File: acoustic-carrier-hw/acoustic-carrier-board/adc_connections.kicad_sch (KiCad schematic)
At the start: 28 parts, among them IC1 ECP5-BGA256, J2 Conn_02x08_Odd_Even, U7 MS9280

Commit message: [carrier] Reorganized schematic, moPut adc signals in bus, fixed DRC errors (next) recheck ethernet, check usb, add power switch
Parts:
- added C108: 10uF, Capacitor_SMD:C_0603_1608Metric, symbol Device:C_Small
- added C109, C136: 0.1uF, Capacitor_SMD:C_0402_1005Metric, symbol Device:C_Small
- added C110: 10nF, Capacitor_SMD:C_0402_1005Metric, symbol Device:C_Small
- added C111, C115, C133: 10pF, Capacitor_SMD:C_0603_1608Metric, symbol Device:C_Small
- added C134, C135: 100 nF +-5%, Capacitor_SMD:C_0603_1608Metric_Pad1.08x0.95mm_HandSolder, symbol Device:C_Small
- added C142: 220nF, Capacitor_SMD:C_0402_1005Metric, symbol Device:C_Small
- added J15, J17, J18, J19, J20, J21, J4: BWU.FL-IPEX1, fpga:BWU.FL-IPEX1, symbol Connector:Conn_Coaxial_Small
- added J22: 8P8C_Shielded, Connector_RJ:RJ45_RCH_RC01937, symbol Connector:8P8C_Shielded
- added R125: 0, Resistor_SMD:R_0603_1608Metric_Pad0.98x0.95mm_HandSolder, symbol Device:R_Small
- added R126, R127, R128, R129: 470, Resistor_SMD:R_0603_1608Metric, symbol Device:R_Small
- added R130, R134, R135, R136, R138, R140, R141, R143, R145, R146: 0, Resistor_SMD:R_0603_1608Metric, symbol Device:R_Small
- added R131, R133, R147, R148, R150, R151: 10k, Resistor_SMD:R_0603_1608Metric, symbol Device:R_Small
- added R132, R137, R144, R149, R152, R154, R156, R157: 1k, Resistor_SMD:R_0603_1608Metric, symbol Device:R_Small
- added R139, R142: 47, Resistor_SMD:R_0603_1608Metric, symbol Device:R_Small
- added R153: 75, Resistor_SMD:R_0603_1608Metric, symbol Device:R_Small
- added R155: 1.5k, Resistor_SMD:R_0603_1608Metric, symbol Device:R_Small
- added R158: 4.7k, Resistor_SMD:R_0603_1608Metric, symbol Device:R_Small
- added RJ2: HR913550A, rj45:RJ45-TH_HR913550A, symbol RJ45_HR913550A:HR913550A
- added TP13, TP14, TP15, TP16, TP17: TestPoint_Small, TestPoint:TestPoint_Pad_D1.5mm, symbol Connector:TestPoint_Small
- added U20: THS4521IDGK, Package_SO:VSSOP-8_3x3mm_P0.65mm, symbol Amplifier_Difference:THS4521IDGK
- added U21: DGQ2788AEN-T1-GE4, fpga:QFN40P260X180X60-16N_Fv1.2, symbol DGQ2788AEN:DGQ2788AEN-T1-GE4
- added U22: LMV321, Package_TO_SOT_SMD:SOT-23-5, symbol Amplifier_Operational:LMV321
- added U23: TL432DBZ, Package_TO_SOT_SMD:SOT-23, symbol Reference_Voltage:TL432DBZ
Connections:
- net ADC_AIN+: now also C115.2, R135.1, R140.1
- net ADC_AIN-: now also C115.1, R143.1, R145.1
- net ADC_IN12_SW: now also IC1.E6 (PT20A), U21.14 (IN1-2); no longer IC1.A7 (PT29A/PCLKT0_0)
- net FPGA_LED0: now also R128.2, R129.2
- net FPGA_LED1: now also R126.2, R127.1
- net GND: now also C108.2, C109.2, C110.2, C136.2, C142.1, J15.2 (Ext), J17.2 (Ext), J18.2 (Ext), J19.2 (Ext), J20.2 (Ext), J21.2 (Ext), J22.SH, J4.2 (Ext), R125.1, R127.2, R129.1, R156.1, R157.2, R158.2, RJ2.5, RJ2.8 (GND), U20.6 (V_{S-}), U21.2 (GND), U22.2 (V-), U23.3 (A)
- net VCORE_3V3: now also C108.1, C109.1, C110.1, C136.1, R138.2, RJ2.12, RJ2.9, U20.3 (V_{S+}), U22.5 (V+)
- net VDDA: now also R152.1, R154.1, U21.10 (V+)
- net SIG.T_SDA: now reaches IC1.A8 (PT29B/PCLKC0_0)
- net SIG.T_SDA: now also J2.15 (Pin_15)
- net FPGA_ADC_CLK renamed FPGA_ADC.CLK
- net FPGA_ADC_D0 renamed FPGA_ADC.D0
- net FPGA_ADC_D1 renamed FPGA_ADC.D1
- net FPGA_ADC_D2 renamed FPGA_ADC.D2
- net FPGA_ADC_D3 renamed FPGA_ADC.D3
- net FPGA_ADC_D4 renamed FPGA_ADC.D4
- net FPGA_ADC_D5 renamed FPGA_ADC.D5
- net FPGA_ADC_D6 renamed FPGA_ADC.D6
- net FPGA_ADC_D7 renamed FPGA_ADC.D7
- net FPGA_ADC_D8 renamed FPGA_ADC.D8
- net FPGA_ADC_D9 renamed FPGA_ADC.D9
- net FPGA_ADC_OTR renamed FPGA_ADC.OTR
- net SIG_B40V_EN: no longer names the net of IC1.D6 (PT20B)
- net SIG_B40V_EN: no longer J2.11 (Pin_11)
- net SIG_PWM0 renamed SIG.PWM0
- net SIG_PWM1 renamed SIG.PWM1
- net SIG_PWM2 renamed SIG.PWM2
- net SIG_PWM3 renamed SIG.PWM3
- net SIG_S10V_EN renamed SIG.S10V_EN
- net SIG.S10V_EN: now also IC1.C7 (PT27A/PCLKT0_1); no longer IC1.E6 (PT20A)
- net SIG_T_SCL renamed SIG.T_SCL
- net SIG.T_SCL: now also IC1.A7 (PT29A/PCLKT0_0); no longer IC1.C7 (PT27A/PCLKT0_1)
- net SIG_T_SDA renamed SIG.B40_EN
- net SIG.B40_EN: now also J2.11 (Pin_11); no longer J2.15 (Pin_15)
- new net: R155.2, R158.1, U23.1 (REF)
- new net: J19.1 (In), U21.4 (COM3)
- new net: J15.1 (In), R133.2, R135.2
- new net: R134.2, R136.1, R137.2
- new net: R136.2, U21.12 (COM1)
- new net: RJ2.3, TP13.1
- new net: C133.1, R144.1, R149.1, U20.1 (-)
- new net: C133.2, R142.2, U20.4
- new net: C111.1, R139.2, U20.5
- new net: R138.1, U20.7 (~{PD})
- new net: C111.2, R132.2, R137.1, U20.8 (+)
- new net: C134.2, R150.2, U21.11 (NO1)
- new net: R141.1, R144.2, R146.1
- new net: R141.2, U21.16 (COM2)
- new net: J4.1 (In), R131.2, R134.1
- new net: R132.1, R139.1, R140.2
- new net: C134.1, J22.5
- new net: RJ2.2, U21.1 (NC2)
- new net: RJ2.1, U21.13 (NC1)
- new net: C135.2, R151.1, U21.15 (NO2)
- new net: J18.1 (In), U21.3 (NO3)
- new net: J17.1 (In), U21.5 (NC3)
- new net: TP15.1, U21.6 (IN3-4)
- new net: RJ2.6, TP14.1
- new net: J20.1 (In), R145.2, R147.2
- new net: R125.2, RJ2.13, RJ2.14
- new net: R142.1, R143.2, R149.2
- new net: J21.1 (In), R146.2, R148.2
- new net: R130.2, RJ2.4
- new net: J22.2, TP16.1
- new net: R128.1, RJ2.10
- new net: R126.1, RJ2.11
- new net: R153.2, R156.2, U22.3 (-), U22.4
- new net: J22.1, TP17.1
- new net: C135.1, J22.4
- new net ADC_VOCM_BUFF: C142.2, R130.1, R131.1, R133.1, R147.1, R148.1, R150.1, R151.2, R153.1, U20.2 (V_{OCM})
- new net ADC_VOCM_REF: R152.2, R154.2, R155.1, R157.1, U22.1 (+), U23.2 (K)
- no-connect marks 1 -> 9
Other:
- note added: "- Ethernet magnetics by default for decoupling Layout of transition between 2 ADC-inputs: - Use 0-ohm resistor to cross lower trace (instead of jumpers for signal integrity) LEDS: - Current through leds (3.3 - 2.2) / 2e3 = 0.55 mA (voltage drop 1.8-2.8 V) - Differential impedance: 100 ohms - Input capacitance: 100 nF, f_plateau = 1/[2*pi*C*(R_diff/2)] = 30 kHz Pin 13, 14: shield / frame connection"
- note added: "ADC CONNECTORS"
- note added: "ADC Filter - Optimize later with signal generator + measurements - Input impedance (max 100 kOhm) >>> then source (100 ohm)"
- note added: "ADC INPUT BUFFER"
- note added: "ADC LOW PASS FILTER"
- note added: "ADC SWITCH"
- note added: "Current requirement in nA - Current limiting resistor -> smaller = less noise -> larger = less energy wasting - Reference input current: 0.6 uA - 3.3e-3 / (1+1.5+4.7) = 532 uA through biasing resistors - (3.3-1.65) / 1k = 1.65 mA flowing through the Cathode"
- note added: "Secondary voltage divider reference (just in case the reference doesn't work)"
- note added: "Test connector Make stub as short as possible"
- note added: "VOCM REFERENCE BUFFERING"
- note added: "VOCM REFERENCE GENERATION"
- note added: "VOCM buffering - Reducing source impedance of resistive divider - buffer configuration for OPAMP to drive COMP pin - Damping resistor added at output due to big capacitive load - Maximum output current: 5-40 mA - Maximum current: 1.6 V / 75 ohms = 21.33 mA Differential mode biasing - 10 kOhm, 0.80 uA input bias for ths4521 -> 10e3 * 0.80e-6 = 8 mV offset at worst Use LMV321 - Higher current than 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"
- note added: "Voltage reference: 1.25 Target voltage: 1.65 So Vtarget * [R1/(R1+R2)]= Vref - R1: 1.5k, R2: 4.6k - Vref * R1/(R1+R2) = Vtarget * [4.6/(1.5+4.6)] = Vref - Deviation from 1.25: (1.25-1.244/1.25) = 0.48%"
- moved on the sheet: C86, C87, C88, C89, C90, C91, C92, C93, C94, C95, IC1B, J2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

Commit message: [carrier] Fixed error in ethernet power supply, separated footprints + symbols into library (next) check whether supply should be DVDDH
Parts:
- removed IC1: ECP5-BGA256, fpga:BGA256C80P16X16_1400X1400X170, symbol ecp5bga256:ECP5-BGA256
- removed J15, J18, J19, J20, J21: BWU.FL-IPEX1, fpga:BWU.FL-IPEX1, symbol Connector:Conn_Coaxial_Small
- removed RJ2: HR913550A, rj45:RJ45-TH_HR913550A, symbol RJ45_HR913550A:HR913550A
- removed U21: DGQ2788AEN-T1-GE4, fpga:QFN40P260X180X60-16N_Fv1.2, symbol DGQ2788AEN:DGQ2788AEN-T1-GE4
- removed U7: MS9280, Package_SO:SSOP-28_5.3x10.2mm_P0.65mm, symbol ms9280:MS9280
- added IC1: ECP5-BGA256, iw-fpga_mcu:BGA256C80P16X16_1400X1400X170, symbol iw-fpga_mcu:ECP5-BGA256
- added J1, J10, J11, J5, J7: BWU.FL-IPEX1, iw-connector:BWU.FL-IPEX1, symbol Connector:Conn_Coaxial_Small
- added RJ1: HR913550A, iw-connector:RJ45-TH_HR913550A, symbol iw-connector:HR913550A
- added U2: DGQ2788AEN-T1-GE4, iw-analog:QFN40P260X180X60-16N_Fv1.2, symbol iw-analog:DGQ2788AEN-T1-GE4
- added U3: MS9280, Package_SO:SSOP-28_5.3x10.2mm_P0.65mm, symbol iw-analog:MS9280
- J17, J4: footprint fpga:BWU.FL-IPEX1 -> iw-connector:BWU.FL-IPEX1
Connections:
- net ADC_AIN+: now also U3.27 (AIN)
- net ADC_IN12_SW: now also IC1.E6 (PT20A), U2.14 (IN1-2)
- net ADC_MODE: now also U3.23 (MODE)
- net ADC_REFBF: now also U3.24 (REFBF)
- net ADC_REFBS: now also U3.25 (REFBS)
- net ADC_REFSENSE: now also U3.18 (REFSENSE)
- net ADC_REFTF: now also U3.22 (REFTF)
- net ADC_REFTS: now also U3.21 (REFTS)
- net ADC_VREF: now also U3.26 (VREF)
- net FPGA_ADC.CLK: now also IC1.A2 (PT4A), U3.15 (CLK)
- net FPGA_ADC.D0: now also IC1.B3 (PT4B), U3.3 (D0)
- net FPGA_ADC.D1: now also IC1.A3 (PT6A), U3.4 (D1)
- net FPGA_ADC.D2: now also IC1.A4 (PT6B), U3.5 (D2)
- net FPGA_ADC.D3: now also IC1.E4 (PT9A), U3.6 (D3)
- net FPGA_ADC.D4: now also IC1.D4 (PT9B), U3.7 (D4)
- net FPGA_ADC.D5: now also IC1.C4 (PT11A), U3.8 (D5)
- net FPGA_ADC.D6: now also IC1.B4 (PT11B), U3.9 (D6)
- net FPGA_ADC.D7: now also IC1.E5 (PT13A), U3.10 (D7)
- net FPGA_ADC.D8: now also IC1.D5 (PT13B), U3.11 (D8)
- net FPGA_ADC.D9: now also IC1.C5 (PT15A), U3.12 (D9)
- net FPGA_ADC.OTR: now also IC1.B5 (PT15B), U3.13 (OTR)
- net FPGA_LED0: now also IC1.A6 (PT18B)
- net FPGA_LED1: now also IC1.A5 (PT18A)
- net GND: now also J1.2 (Ext), J10.2 (Ext), J11.2 (Ext), J5.2 (Ext), J7.2 (Ext), RJ1.5, RJ1.8 (GND), U2.2 (GND), U3.1 (AVSS), U3.14 (DRVSS), U3.19 (CLAMP)
- net SIG.B40_EN: now also IC1.B7 (PT27B/PCLKC0_1)
- net SIG.PWM0: now also IC1.C6 (PT22A)
- net SIG.PWM1: now also IC1.B6 (PT22B)
- net SIG.PWM2: now also IC1.E7 (PT24A/GR_PCLK0_1)
- net SIG.PWM3: now also IC1.D7 (PT24B/GR_PCLK0_0)
- net SIG.S10V_EN: now also IC1.C7 (PT27A/PCLKT0_1)
- net SIG.T_SCL: now also IC1.A7 (PT29A/PCLKT0_0)
- net SIG.T_SDA: now also IC1.A8 (PT29B/PCLKC0_0)
- net VCORE_3V3: now also IC1.F6 (VCCIO0_1), IC1.F7 (VCCIO0_2), RJ1.12, RJ1.9, U3.2 (DRVDD)
- net VDDA: now also U2.10 (V+), U3.28 (AVDD)
- net at R133.2, R135.2: now also J10.1 (In)
- net at R136.2: now also U2.12 (COM1)
- net at TP13.1: now also RJ1.3
- net at C134.2, R150.2: now also U2.11 (NO1)
- net at R141.2: now also U2.16 (COM2)
- net at R79.2: now also U3.20 (CLAMPIN)
- net at JP6.2 (B): now also U3.16 (TRISTATE), U3.17 (STBY)
- net at C135.2, R151.1: now also U2.15 (NO2)
- net at J17.1 (In): now also U2.5 (NC3)
- net at TP15.1: now also U2.6 (IN3-4)
- net at TP14.1: now also RJ1.6
- net at R145.2, R147.2: now also J11.1 (In)
- net at R125.2: now also RJ1.13, RJ1.14
- net at R146.2, R148.2: now also J7.1 (In)
- net at R130.2: now also RJ1.4
- net at R128.1: now also RJ1.10
- net at R126.1: now also RJ1.11
- new net: RJ1.1, U2.13 (NC1)
- new net: RJ1.2, U2.1 (NC2)
- new net: J5.1 (In), U2.4 (COM3)
- new net: J1.1 (In), U2.3 (NO3)
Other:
- moved on the sheet: C134, C135, J22, R150, R151, TP16, TP17

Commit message: [carrier] Signal switch-around in ddr3
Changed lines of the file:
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@@
 	(wire
 		(pts
-			(xy 142.24 212.09) (xy 142.24 210.82)
+			(xy 142.24 212.09) (xy 142.24 215.9)
 		)
 		(stroke
@@
 		)
 		(property "Value" "100 nF +-5%"
-			(at 54.102 109.22 90)
+			(at 49.022 122.174 0)
 			(effects
 				(font
@@
 		(dnp no)
 		(property "Reference" "C135"
-			(at 45.466 122.428 0)
+			(at 47.498 126.492 0)
 			(effects
 				(font
@@
 		)
 		(property "Value" "100 nF +-5%"
-			(at 54.102 116.84 90)
+			(at 41.402 132.588 0)
 			(effects
 				(font
@@
 	(symbol
 		(lib_id "power:GND")
-		(at 142.24 210.82 180)
+		(at 142.24 215.9 0)
 		(unit 1)
 		(exclude_from_sim no)
@@
 		(dnp no)
 		(property "Reference" "#PWR030"
-			(at 142.24 204.47 0)
+			(at 142.24 222.25 0)
 			(effects
 				(font
@@
 		)
 		(property "Value" "GND"
-			(at 146.05 209.804 0)
+			(at 138.43 216.916 0)
 			(effects
 				(font
@@
 		)
 		(property "Footprint" ""
-			(at 142.24 210.82 0)
+			(at 142.24 215.9 0)
 			(effects
 				(font
@@
 		)
 		(property "Datasheet" ""
-			(at 142.24 210.82 0)
+			(at 142.24 215.9 0)
 			(effects
 				(font
@@
 		)
 		(property "Description" "Power symbol creates a global label with name \"GND\" , ground"
-			(at 142.24 210.82 0)
+			(at 142.24 215.9 0)
 			(effects
 				(font

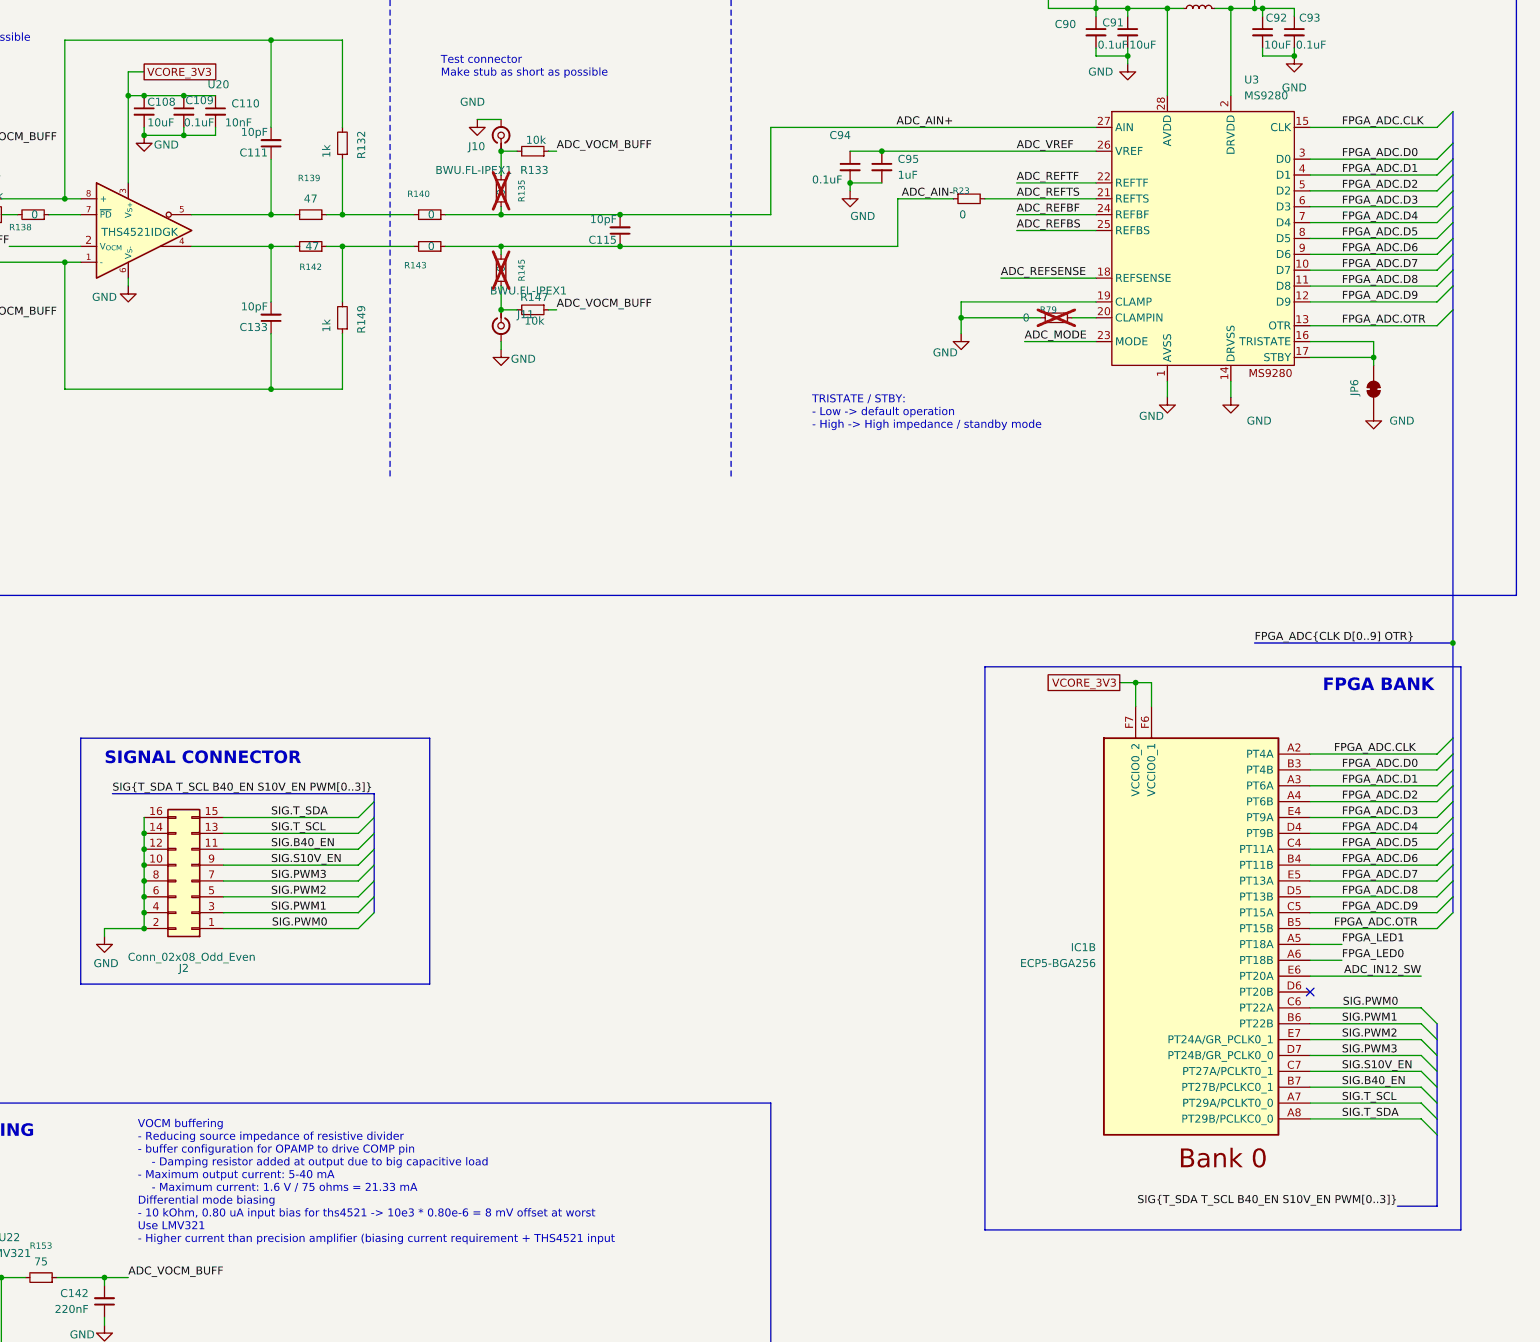
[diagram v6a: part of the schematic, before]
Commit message: [¢arrier] Fixed busses, added resistive arrays instead of 4x4k7 or 4x10k
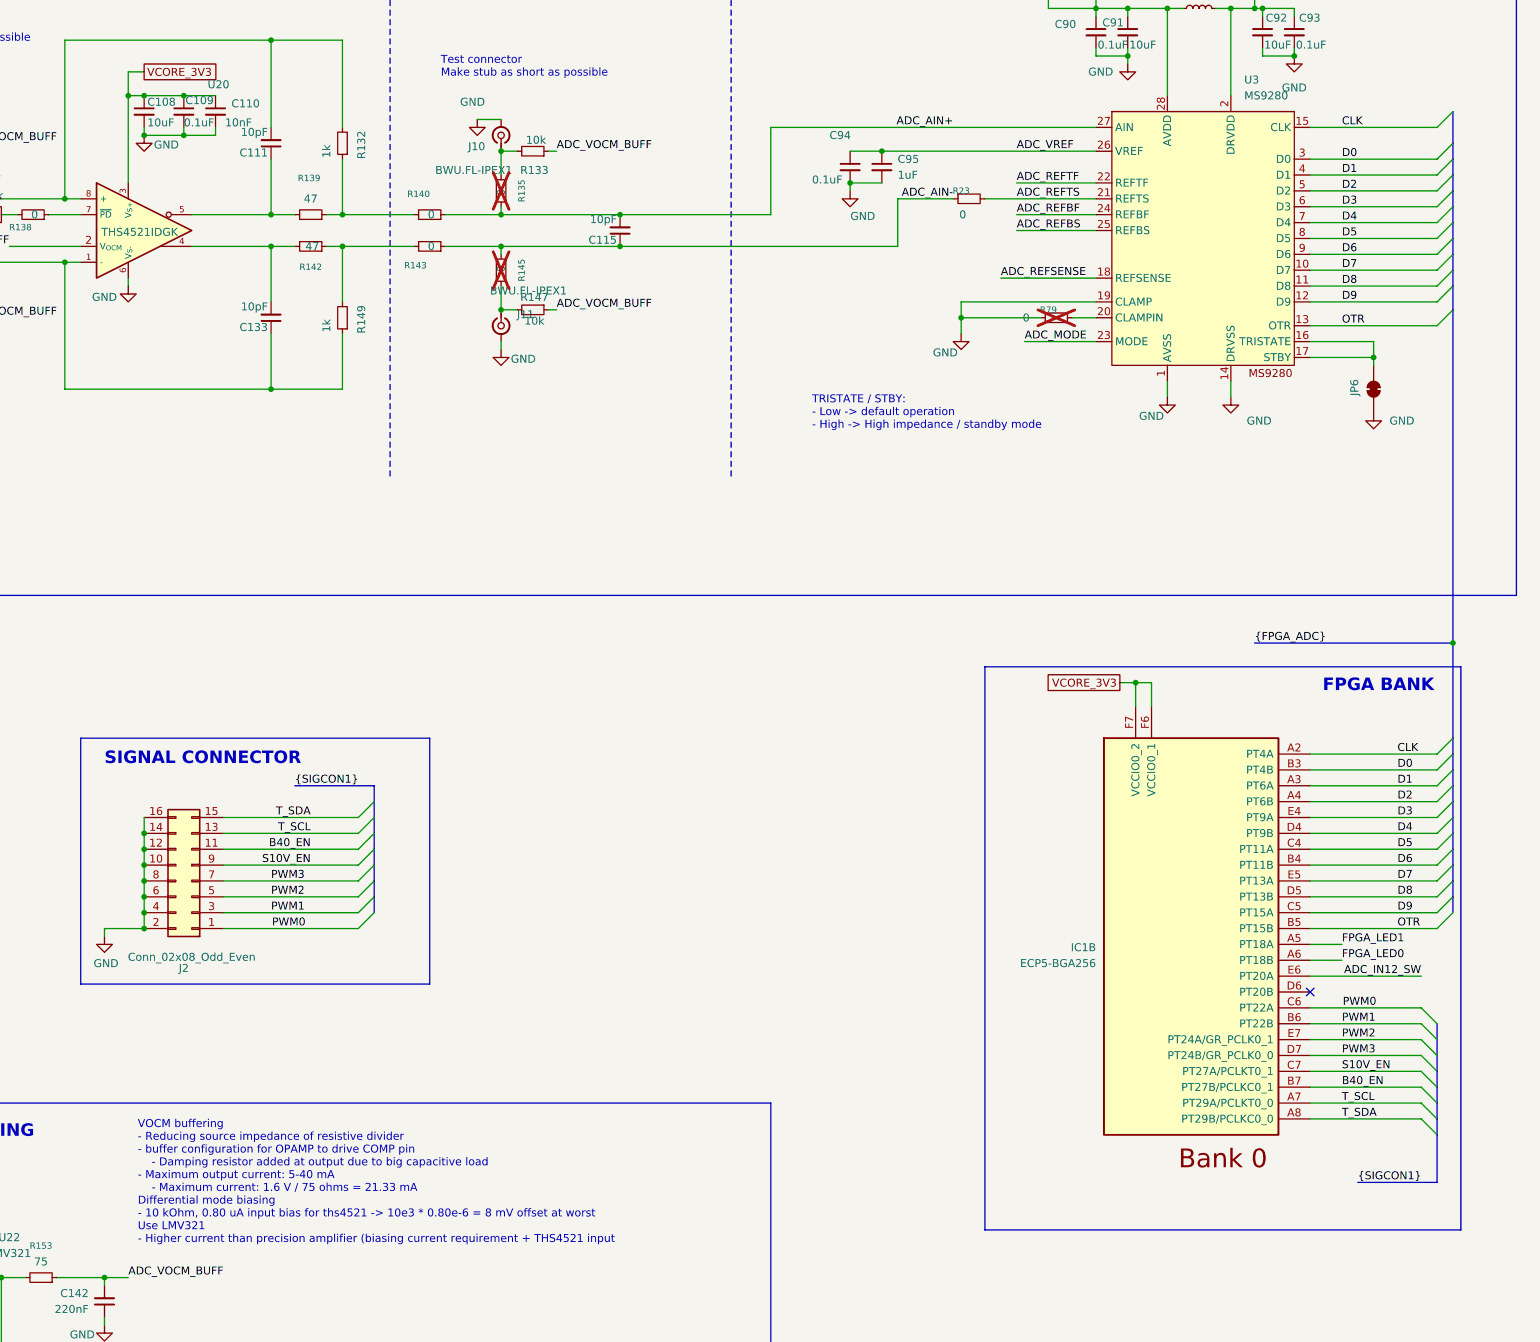
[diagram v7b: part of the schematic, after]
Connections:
- net FPGA_ADC.CLK renamed CLK
- net FPGA_ADC.D0 renamed D0
- net FPGA_ADC.D1 renamed D1
- net FPGA_ADC.D2 renamed D2
- net FPGA_ADC.D3 renamed D3
- net FPGA_ADC.D4 renamed D4
- net FPGA_ADC.D5 renamed D5
- net FPGA_ADC.D6 renamed D6
- net FPGA_ADC.D7 renamed D7
- net FPGA_ADC.D8 renamed D8
- net FPGA_ADC.D9 renamed D9
- net FPGA_ADC.OTR renamed OTR
- net SIG.B40_EN renamed B40_EN
- net SIG.PWM0 renamed PWM0
- net SIG.PWM1 renamed PWM1
- net SIG.PWM2 renamed PWM2
- net SIG.PWM3 renamed PWM3
- net SIG.S10V_EN renamed S10V_EN
- net SIG.T_SCL renamed T_SCL
- net SIG.T_SDA renamed T_SDA
